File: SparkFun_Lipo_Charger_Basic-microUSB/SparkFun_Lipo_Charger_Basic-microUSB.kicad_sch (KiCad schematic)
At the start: 16 parts, among them U1 MCP73831

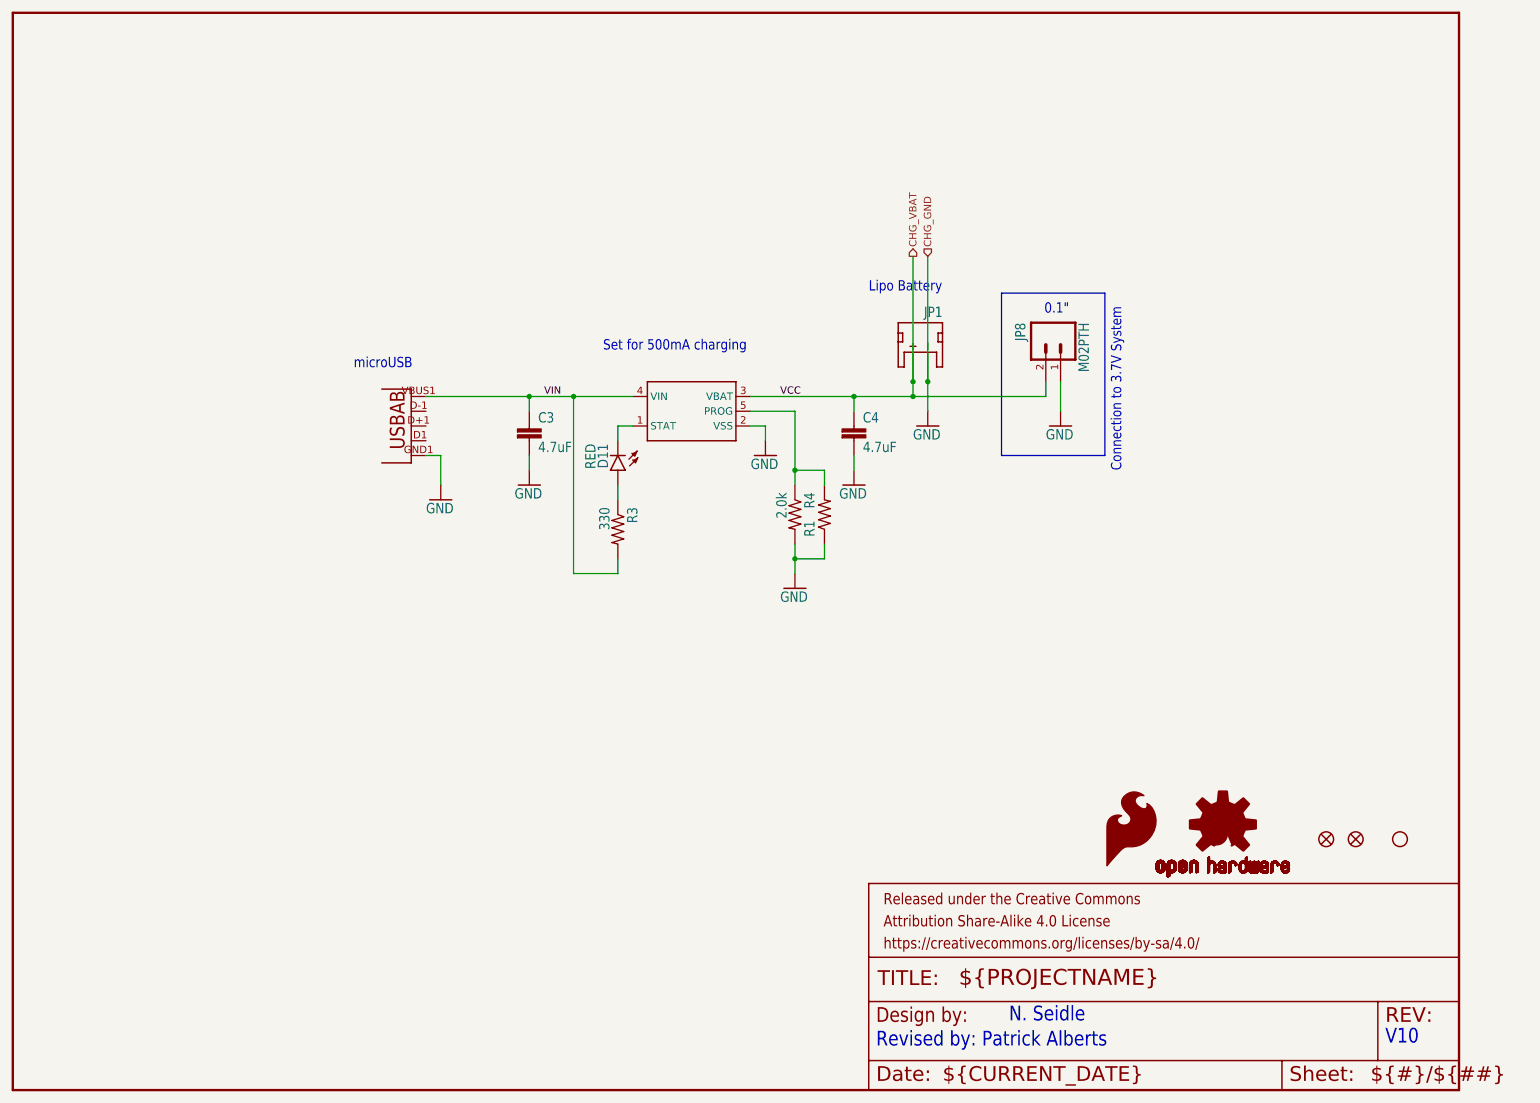
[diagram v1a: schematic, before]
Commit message: update schematic
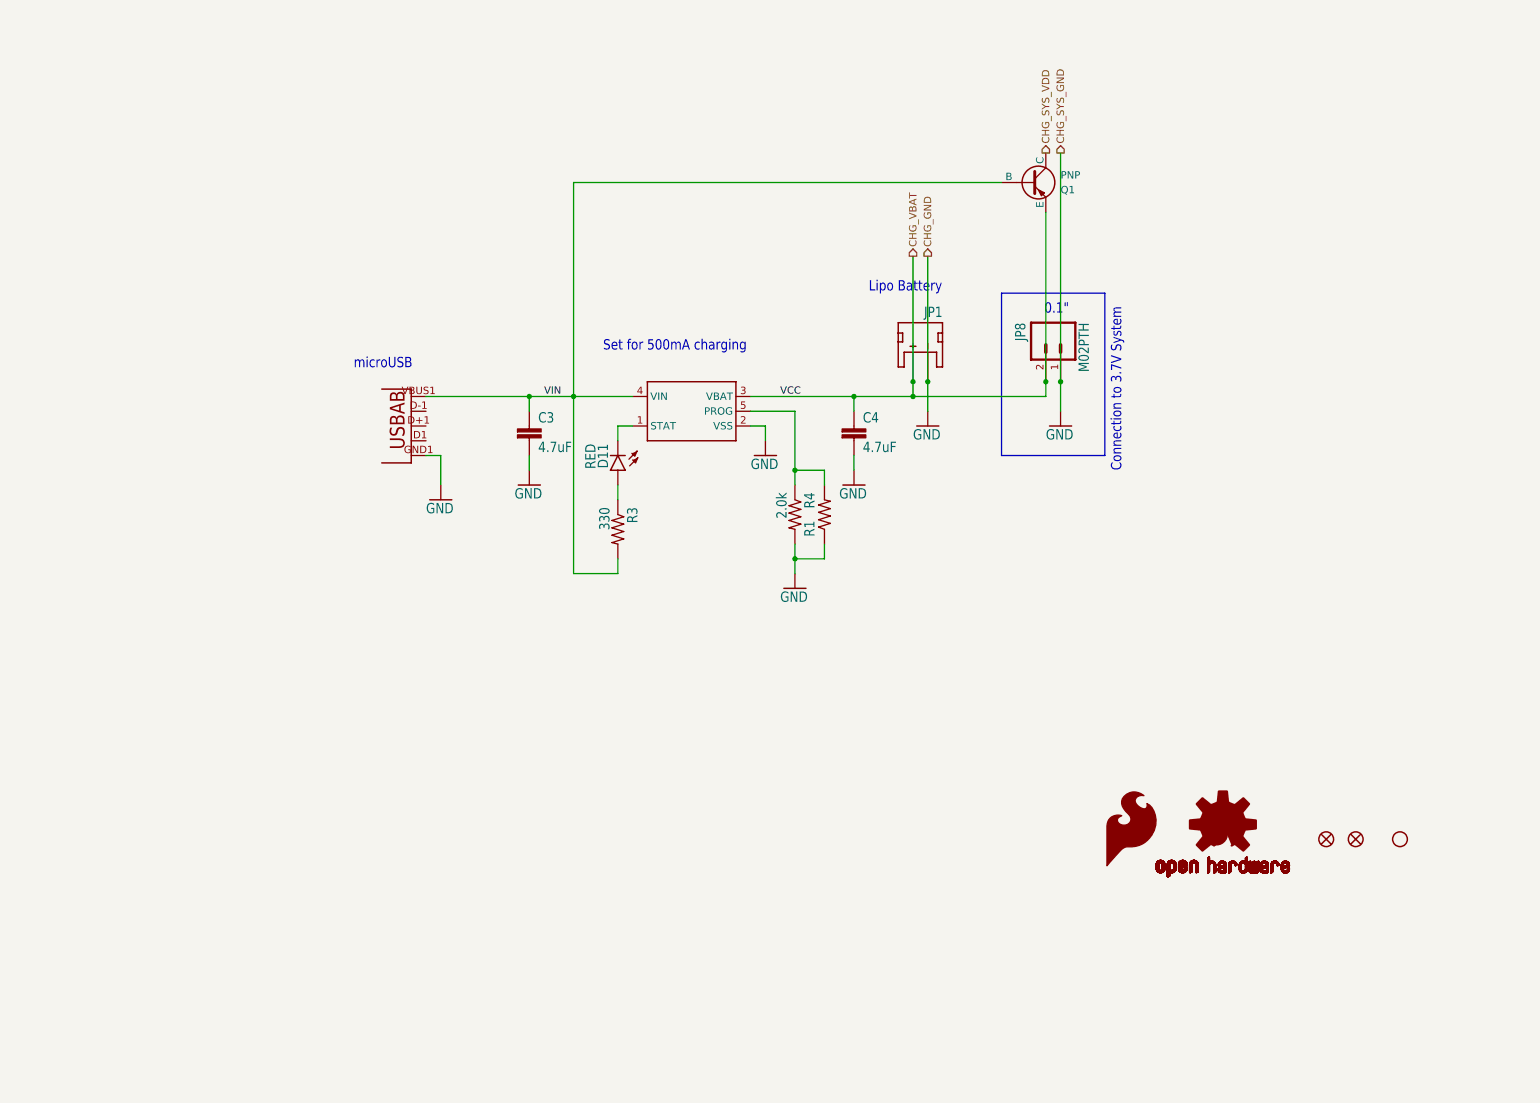
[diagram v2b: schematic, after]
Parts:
- removed FRAME1: FRAME-LETTER, SparkFun_Lipo_Charger_Basic-microUSB:CREATIVE_COMMONS, symbol SparkFun_Lipo_Charger_Basic-microUSB-eagle-import:FRAME-LETTER
- added Q1: PNP, symbol Simulation_SPICE:PNP
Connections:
- net CHG_VBAT: now also Q1.3 (E)
- net VIN: now also Q1.2 (B)
- new net CHG_SYS_VDD: Q1.1 (C)
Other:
- note removed: "N. Seidle"
- note removed: "Revised by: Patrick Alberts"
- note removed: "V10"
- company: (none) -> PFPU2
- title: (none) -> LiPo Charger
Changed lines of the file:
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@@
 (kicad_sch (version 20230121) (generator eeschema)
-  (paper "User" 297.002 223.926)
+  (paper "A4")
+  (title_block
+    (title "LiPo Charger")
+    (date "2024-03-24")
+    (rev "3")
+    (company "PFPU2")
+    (comment 1 "Released under CC BY-SA 4.0")
+    (comment 2 "Original schematic from https://www.sparkfun.com/products/10217")
+  )
+  (junction (at 198.12 81.28) (diameter 0) (color 0 0 0 0)
+  )
   (junction (at 165.1 83.82) (diameter 0) (color 0 0 0 0)
   )
@@
   )
   (junction (at 109.22 83.82) (diameter 0) (color 0 0 0 0)
+  )
+  (junction (at 200.66 81.28) (diameter 0) (color 0 0 0 0)
   )
   (junction (at 154.94 96.52) (diameter 0) (color 0 0 0 0)
@@
     (stroke (width 0.1524) (type solid))
   )
+  (wire (pts (xy 198.12 52.07) (xy 198.12 81.28))
+    (stroke (width 0) (type default))
+  )
   (wire (pts (xy 175.26 59.69) (xy 175.26 81.28))
     (stroke (width 0) (type default))
   )
+  (wire (pts (xy 124.46 111.76) (xy 124.46 114.3))
+    (stroke (width 0.1524) (type solid))
+  )
   (wire (pts (xy 154.94 114.3) (xy 154.94 111.76))
     (stroke (width 0.1524) (type solid))
   )
-  (wire (pts (xy 124.46 111.76) (xy 124.46 114.3))
+  (wire (pts (xy 124.46 88.9) (xy 124.46 91.44))
     (stroke (width 0.1524) (type solid))
   )
@@
     (stroke (width 0.2032) (type solid))
   )
+  (wire (pts (xy 116.84 83.82) (xy 116.84 46.99))
+    (stroke (width 0.1524) (type solid))
+  )
+  (wire (pts (xy 116.84 46.99) (xy 190.5 46.99))
+    (stroke (width 0.1524) (type solid))
+  )
   (wire (pts (xy 127 88.9) (xy 124.46 88.9))
     (stroke (width 0.1524) (type solid))
@@
     (stroke (width 0.1524) (type solid))
   )
+  (wire (pts (xy 200.66 41.91) (xy 200.66 81.28))
+    (stroke (width 0.1524) (type solid))
+  )
+  (wire (pts (xy 124.46 99.06) (xy 124.46 101.6))
+    (stroke (width 0) (type default))
+  )
   (wire (pts (xy 154.94 86.36) (xy 154.94 96.52))
-    (stroke (width 0.1524) (type solid))
-  )
-  (wire (pts (xy 124.46 88.9) (xy 124.46 91.44))
     (stroke (width 0.1524) (type solid))
   )
@@
     (stroke (width 0.1524) (type solid))
   )
-  (wire (pts (xy 124.46 101.6) (xy 124.46 99.06))
-    (stroke (width 0.1524) (type solid))
-  )
   (wire (pts (xy 198.12 81.28) (xy 198.12 83.82))
     (stroke (width 0.1524) (type solid))
@@
     (effects (font (size 1.778 1.5113)) (justify left bottom))
   )
-  (text "Revised by: Patrick Alberts" (at 168.91 196.088 0)
-    (effects (font (size 2.54 2.159)) (justify left bottom))
-  )
-  (text "N. Seidle" (at 191.77 191.77 0)
-    (effects (font (size 2.54 2.159)) (justify left bottom))
-  )
   (text "0.1\"" (at 197.866 69.85 0)
     (effects (font (size 1.778 1.5113)) (justify left bottom))
@@
     (effects (font (size 1.778 1.5113)) (justify left bottom))
   )
-  (text "V10" (at 256.54 195.58 0)
-    (effects (font (size 2.54 2.159)) (justify left bottom))
-  )
   (text "microUSB" (at 78.994 79.248 0)
     (effects (font (size 1.778 1.5113)) (justify left bottom))
@@
     (effects (font (size 1.2446 1.2446)) (justify left bottom))
   )
-  (hierarchical_label "CHG_GND" (shape input) (at 177.8 59.69 90) (fields_autoplaced)
+  (hierarchical_label "CHG_GND" (shape output) (at 177.8 59.69 90) (fields_autoplaced)
     (effects (font (size 1.27 1.27)) (justify left))
   )
   (hierarchical_label "CHG_VBAT" (shape output) (at 175.26 59.69 90) (fields_autoplaced)
+    (effects (font (size 1.27 1.27)) (justify left))
+  )
+  (hierarchical_label "CHG_SYS_GND" (shape output) (at 200.66 41.91 90) (fields_autoplaced)
+    (effects (font (size 1.27 1.27)) (justify left))
+  )
+  (hierarchical_label "CHG_SYS_VDD" (shape output) (at 198.12 41.91 90) (fields_autoplaced)
     (effects (font (size 1.27 1.27)) (justify left))
   )
@@
     )
   )
-  (symbol (lib_id "SparkFun_Lipo_Charger_Basic-microUSB-eagle-import:FRAME-LETTER") (at 167.64 203.2 0) (unit 2)
-    (in_bom yes) (on_board yes) (dnp no)
-    (property "Reference" "FRAME1" (at 167.64 203.2 0)
-      (effects (font (size 1.27 1.27)) hide)
-    )
-    (property "Value" "FRAME-LETTER" (at 167.64 203.2 0)
-      (effects (font (size 1.27 1.27)) hide)
-    )
-    (property "Footprint" "SparkFun_Lipo_Charger_Basic-microUSB:CREATIVE_COMMONS" (at 167.64 203.2 0)
-      (effects (font (size 1.27 1.27)) hide)
-    )
-    (property "Datasheet" "" (at 167.64 203.2 0)
-      (effects (font (size 1.27 1.27)) hide)
-    )
-    (instances
-      (project "SparkFun_Lipo_Charger_Basic-microUSB"
-        (path "/342e9741-5281-407b-be73-39ccad418930"
-          (reference "FRAME1") (unit 2)
-        )
-      )
-      (project "aps490_detection"
-        (path "/e118c919-9296-4265-a7f4-7c13f94290b1/bad03448-3ebc-42d0-be48-dd19294cc20c/0189be23-f30a-49a0-a245-8d28dabd251c"
-          (reference "FRAME1") (unit 2)
-        )
-      )
-    )
-  )
   (symbol (lib_id "SparkFun_Lipo_Charger_Basic-microUSB-eagle-import:GND") (at 149.86 93.98 0) (unit 1)
     (in_bom yes) (on_board yes) (dnp no)
@@
     )
   )
+  (symbol (lib_id "Simulation_SPICE:PNP") (at 195.58 46.99 0) (unit 1)
+    (in_bom yes) (on_board yes) (dnp no)
+    (property "Reference" "Q1" (at 200.66 48.26 0)
+      (effects (font (size 1.27 1.27)) (justify left))
+    )
+    (property "Value" "PNP" (at 200.66 45.72 0)
+      (effects (font (size 1.27 1.27)) (justify left))
+    )
+    (property "Footprint" "" (at 231.14 46.99 0)
+      (effects (font (size 1.27 1.27)) hide)
+    )
+    (property "Datasheet" "https://ngspice.sourceforge.io/docs/ngspice-html-manual/manual.xhtml#cha_BJTs" (at 231.14 46.99 0)
+      (effects (font (size 1.27 1.27)) hide)
+    )
+    (property "Sim.Device" "PNP" (at 195.58 46.99 0)
+      (effects (font (size 1.27 1.27)) hide)
+    )
+    (property "Sim.Type" "GUMMELPOON" (at 195.58 46.99 0)
+      (effects (font (size 1.27 1.27)) hide)
+    )
+    (property "Sim.Pins" "1=C 2=B 3=E" (at 195.58 46.99 0)
+      (effects (font (size 1.27 1.27)) hide)
+    )
+    (pin "1")
+    (pin "2")
+    (pin "3")
+    (instances
+      (project "aps490_detection"
+        (path "/e118c919-9296-4265-a7f4-7c13f94290b1/bad03448-3ebc-42d0-be48-dd19294cc20c/0189be23-f30a-49a0-a245-8d28dabd251c"
+          (reference "Q1") (unit 1)
+        )
+      )
+    )
+  )
   (symbol (lib_id "SparkFun_Lipo_Charger_Basic-microUSB-eagle-import:FIDUCIAL1X2") (at 246.38 160.02 0) (unit 1)
     (in_bom yes) (on_board yes) (dnp no)
@@
         )
       )
-    )
-  )
-  (symbol (lib_id "SparkFun_Lipo_Charger_Basic-microUSB-eagle-import:FRAME-LETTER") (at 20.32 203.2 0) (unit 1)
-    (in_bom yes) (on_board yes) (dnp no)
-    (property "Reference" "FRAME1" (at 20.32 203.2 0)
-      (effects (font (size 1.27 1.27)) hide)
-    )
-    (property "Value" "FRAME-LETTER" (at 20.32 203.2 0)
-      (effects (font (size 1.27 1.27)) hide)
-    )
-    (property "Footprint" "SparkFun_Lipo_Charger_Basic-microUSB:CREATIVE_COMMONS" (at 20.32 203.2 0)
-      (effects (font (size 1.27 1.27)) hide)
-    )
-    (property "Datasheet" "" (at 20.32 203.2 0)
-      (effects (font (size 1.27 1.27)) hide)
-    )
-    (instances
-      (project "SparkFun_Lipo_Charger_Basic-microUSB"
-        (path "/342e9741-5281-407b-be73-39ccad418930"
-          (reference "FRAME1") (unit 1)
-        )
-      )
-      (project "aps490_detection"
-        (path "/e118c919-9296-4265-a7f4-7c13f94290b1/bad03448-3ebc-42d0-be48-dd19294cc20c/0189be23-f30a-49a0-a245-8d28dabd251c"
-          (reference "FRAME1") (unit 1)
-        )
-      )
